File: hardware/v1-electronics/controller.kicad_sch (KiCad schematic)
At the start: 8 parts, among them J3 Female JST-SH, SW8 SW_Push, U1 MDBT50Q-1MV2

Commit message: checkpoint(v1 hardware): this is the save before corrections
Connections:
- net VDD renamed V_REG0
- net V_SYS renamed +5V
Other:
- note added: "Consider if there enough space for UART debug. No there will not be"
- note added: "Low Frequency IO Pins: = P0.02 P0.03 P0.09 P0.10 P0.28 P0.29 P0.30 P0.31 = P1.01 P1.02 P1.03 P1.04 P1.05 P1.06 P1.07 P1.10 = P1.11 P1.12 P1.13 P1.14 P1.15 Standard Frequency IO Pins: = P0.00 P0.01 P0.04 P0.05 P0.06 P0.07 P0.08 P0.11 = P0.12 P0.13 P0.14 P0.15 P0.16 P0.17 P0.18 P0.19 = P0.20 P0.21 P0.22 P0.23 P0.24 P0.25 P0.26 P0.27 = P1.00 P1.08 P1.09 P0.18 is the nRESET Pin. The datasheet is uncl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"
- note added: "Set up resets for the device. Centralize the decoupling for VDDH"
- note added: "VDD is REG0, it defaults to +1V8 and can be set to V_REG0."
- note added: "Verify that this is enough to program this board"
- note removed: "Consider if there enough space for UART debug."
- note removed: "I need 45 pins for I/O, The module exposes 48 io pins I also need reset and bootloading features"
- note removed: "I need to add supporting circuitry I also need to check pin assignments agains the datasheet. (what is and what needs high speed digital io)"
- note removed: "Low Frequency IO Pins: = P0.02 P0.03 P0.09 P0.10 P0.28 P0.29 P0.30 P0.31 = P1.01 P1.02 P1.03 P1.04 P1.05 P1.06 P1.07 P1.10 = P1.11 P1.12 P1.13 P1.14 P1.15 Standard Frequency IO Pins: = P0.00 P0.01 P0.04 P0.05 P0.06 P0.07 P0.08 P0.11 = P0.12 P0.13 P0.14 P0.15 P0.16 P0.17 P0.18 P0.19 = P0.20 P0.21 P0.22 P0.23 P0.24 P0.25 P0.26 P0.27 = P1.00 P1.08 P1.09 P0.18 is the nRESET Pin. Be careful with the p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"
- note removed: "Mention USB here some where"
- note removed: "Set up resets for the device. Centralize the decoupling for V_SYS"
- note removed: "figure where to place these signal if at all. I should probably set ce to ground or disconnected."
- moved on the sheet: C51, SW8

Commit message: fix(v1 hardware): implementing recommendations from Cyril
- rated the lines for the power system
- using a properly rated connecter for the battery
- added manual usb cc detection
- short grounds to each other
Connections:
- net LEDMatrix1Interrupt: no longer U1.47 (P1.00)
- net LEDMatrix1Shutdown: now also U1.8 (P1.15); no longer U1.14 (P0.30)
- net LEDMatrix2Interrupt: no longer U1.8 (P1.15)
- net LEDMatrix2Shutdown: now also U1.47 (P1.00); no longer U1.12 (P0.31)
- net ~{ChargingChipInterrupt}: no longer U1.17 (P0.00)
- new net USB.CC1: U1.14 (P0.30)
- new net USB.CC2: U1.12 (P0.31)
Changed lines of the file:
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@@
 	(title_block
 		(title "Slack")
-		(date "2026-07-12")
-		(rev "A.0.3")
+		(date "2026-07-25")
+		(rev "A.0.4")
 	)
 	(rectangle
@@
 		)
 	)
+	(label "USB.CC2"
+		(at 177.8 76.2 180)
+		(effects
+			(font
+				(size 1.27 1.27)
+			)
+			(justify right)
+		)
+	)
 	(label "RotaryEncoder_BChannel10"
 		(at 177.8 71.12 180)
@@
 		)
 	)
+	(label "USB.CC1"
+		(at 177.8 73.66 180)
+		(effects
+			(font
+				(size 1.27 1.27)
+			)
+			(justify right)
+		)
+	)
 	(label "SWDCLK"
 		(at 25.4 71.12 180)
@@
 		)
 	)
-	(hierarchical_label "LEDMatrix2Shutdown"
-		(shape output)
-		(at 177.8 76.2 180)
-		(effects
-			(font
-				(size 1.27 1.27)
-			)
-			(justify right)
-		)
-	)
-	(hierarchical_label "LEDMatrix2Interrupt"
+	(hierarchical_label "LEDMatrix1Interrupt"
 		(shape input)
-		(at 177.8 132.08 180)
+		(at 104.14 50.8 180)
 		(effects
 			(font
@@
 		)
 	)
+	(hierarchical_label "LEDMatrix2Shutdown"
+		(shape output)
+		(at 218.44 116.84 0)
+		(effects
+			(font
+				(size 1.27 1.27)
+			)
+			(justify left)
+		)
+	)
 	(hierarchical_label "Column[1..14]"
 		(shape output)
@@
 		)
 	)
+	(hierarchical_label "LEDMatrix2Interrupt"
+		(shape input)
+		(at 104.14 48.26 180)
+		(effects
+			(font
+				(size 1.27 1.27)
+			)
+			(justify right)
+		)
+	)
 	(hierarchical_label "~{ChargingChipInterrupt}"
 		(shape input)
-		(at 218.44 55.88 0)
-		(effects
-			(font
-				(size 1.27 1.27)
-			)
-			(justify left)
-		)
-	)
-	(hierarchical_label "LEDMatrix1Shutdown"
-		(shape output)
-		(at 177.8 73.66 180)
-		(effects
-			(font
-				(size 1.27 1.27)
-			)
-			(justify right)
-		)
-	)
-	(hierarchical_label "LEDMatrix1Interrupt"
-		(shape input)
-		(at 218.44 116.84 0)
-		(effects
-			(font
-				(size 1.27 1.27)
-			)
-			(justify left)
+		(at 104.14 53.34 180)
+		(effects
+			(font
+				(size 1.27 1.27)
+			)
+			(justify right)
 		)
 	)
@@
 		)
 	)
+	(hierarchical_label "LEDMatrix1Shutdown"
+		(shape output)
+		(at 177.8 132.08 180)
+		(effects
+			(font
+				(size 1.27 1.27)
+			)
+			(justify right)
+		)
+	)
 	(hierarchical_label "RotaryEncoder_AChannel[1..10]"
 		(shape input)
@@
 		)
 	)
-	(hierarchical_label "USB{D+, D-}"
+	(hierarchical_label "USB{D+, D-, CC1, CC2}"
 		(shape bidirectional)
-		(at 167.64 93.98 180)
-		(effects
-			(font
-				(size 1.27 1.27)
-			)
-			(justify right)
+		(at 83.82 40.64 0)
+		(effects
+			(font
+				(size 1.27 1.27)
+			)
+			(justify left)
 		)
 	)
@@
 		)
 		(pin "14"
+			(alternate "AIN6")
 		)
 		(pin "12"
+			(alternate "AIN7")
 		)
 		(pin "18"

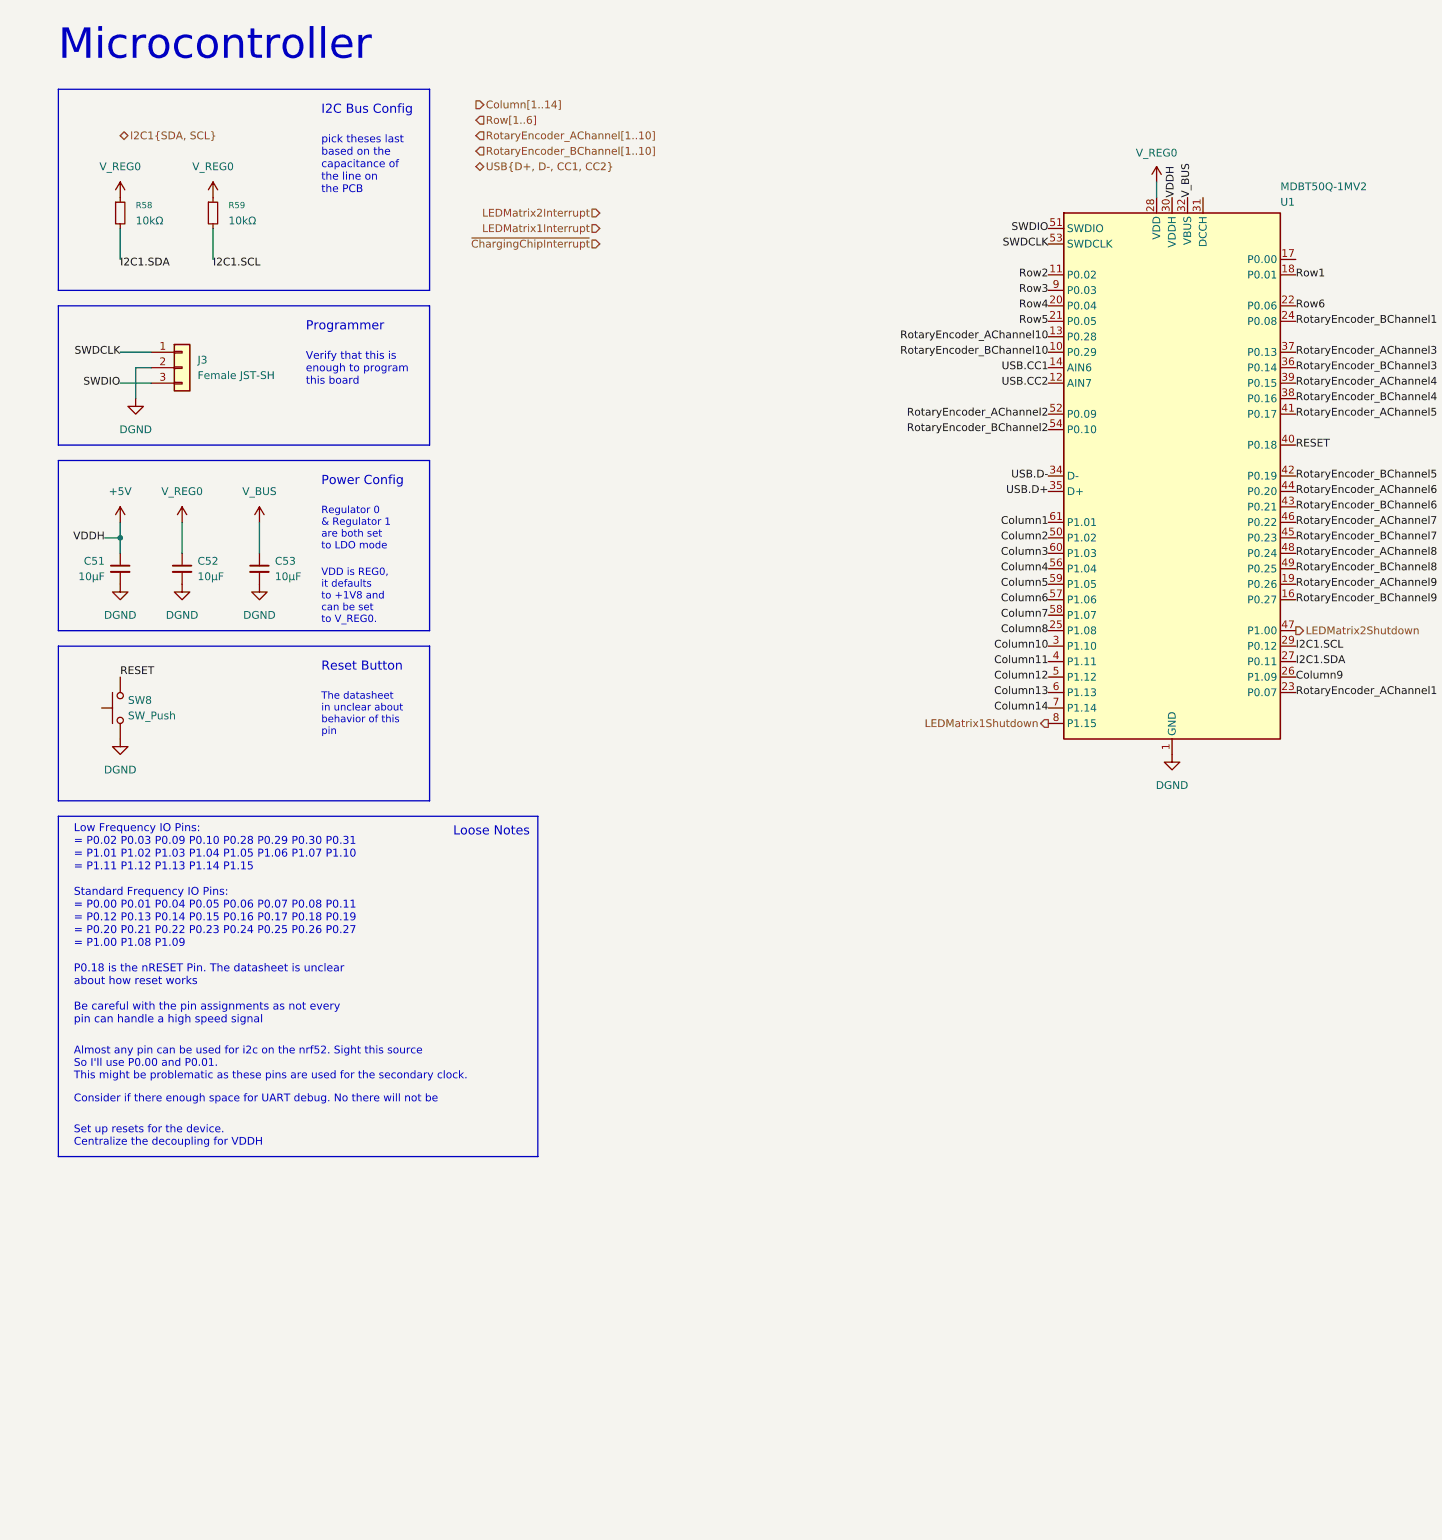
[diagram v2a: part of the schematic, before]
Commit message: fix(v1 hardware): complete set of recommendations
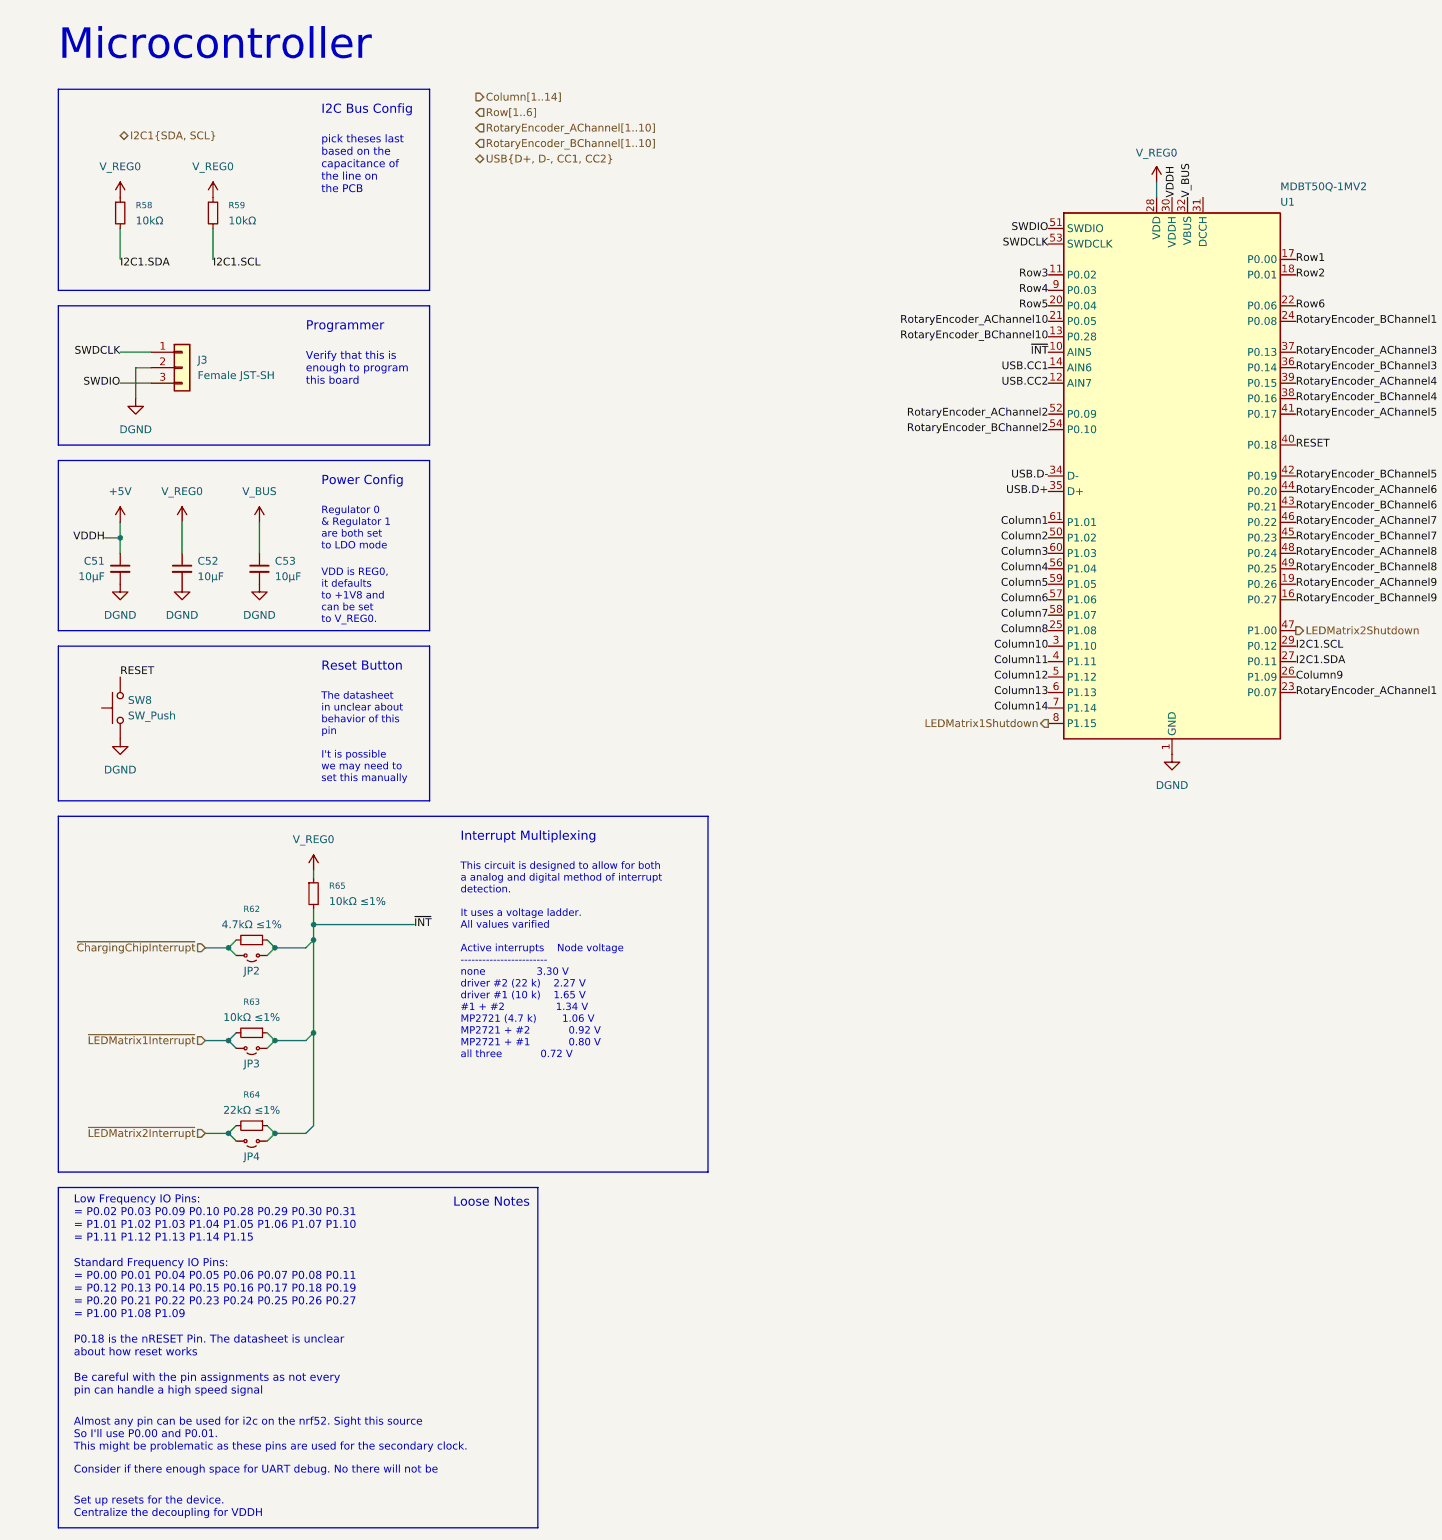
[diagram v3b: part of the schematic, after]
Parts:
- added JP2, JP3, JP4: Jumper_2_Small_Open, symbol Jumper:Jumper_2_Small_Open
- added R62: 4.7kΩ ≤1%, symbol Device:R_Small
- added R63, R65: 10kΩ ≤1%, symbol Device:R_Small
- added R64: 22kΩ ≤1%, symbol Device:R_Small
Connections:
- net RotaryEncoder_AChannel10: now also U1.21 (P0.05); no longer U1.13 (P0.28)
- net RotaryEncoder_BChannel10: now also U1.13 (P0.28); no longer U1.10 (P0.29)
- net Row1: now also U1.17 (P0.00); no longer U1.18 (P0.01)
- net Row2: now also U1.18 (P0.01); no longer U1.11 (P0.02)
- net Row3: now also U1.11 (P0.02); no longer U1.9 (P0.03)
- net Row4: now also U1.9 (P0.03); no longer U1.20 (P0.04)
- net Row5: now also U1.20 (P0.04); no longer U1.21 (P0.05)
- net V_REG0: now also R65.1
- net ~{ChargingChipInterrupt}: now also JP2.2 (B), R62.2
- new net ~{INT}: JP2.1 (A), JP3.1 (A), JP4.1 (A), R62.1, R63.1, R64.1, R65.2, U1.10 (P0.29)
- new net ~{LEDMatrix1Interrupt}: JP3.2 (B), R63.2
- new net ~{LEDMatrix2Interrupt}: JP4.2 (B), R64.2
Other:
- note added: "Interrupt Multiplexing"
- note added: "The datasheet in unclear about behavior of this pin I't is possible we may need to set this manually"
- note added: "This circuit is designed to allow for both a analog and digital method of interrupt detection. It uses a voltage ladder. All values varified Active interrupts Node voltage ------------------------ none 3.30 V driver #2 (22 k) 2.27 V driver #1 (10 k) 1.65 V #1 + #2 1.34 V MP2721 (4.7 k) 1.06 V MP2721 + #2 0.92 V MP2721 + #1 0.80 V all three 0.72 V"
- note removed: "The datasheet in unclear about behavior of this pin"

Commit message: feat(v1 hardware): place foot prints
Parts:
- C51, C52, C53: footprint (none) -> Capacitor_SMD:C_0805_2012Metric
- J3: footprint (none) -> Connector_JST:JST_SH_BM03B-SRSS-TB_1x03-1MP_P1.00mm_Vertical
- JP2, JP3, JP4: footprint (none) -> Connector_PinHeader_2.54mm:PinHeader_1x02_P2.54mm_Vertical
- R58, R59, R62, R63, R64, R65: footprint (none) -> Resistor_SMD:R_0805_2012Metric
- SW8: footprint (none) -> Button_Switch_SMD:SW_Push_1P1T_XKB_TS-1187A
